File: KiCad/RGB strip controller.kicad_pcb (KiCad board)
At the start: 2 copper layers, 17.1 x 48.9 mm, 16 parts, among them J1 USB_C_Receptacle_USB2.0, J2 Conn_01x03, SW1 SW_SPST, U1 ESP-01, U2 LM317_TO-220

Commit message: PCB revision 2
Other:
- board text added: "v2"
- board text added: "←"

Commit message: PCB v3
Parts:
- added U3: TC7SZ125FU, Package_TO_SOT_SMD:SOT-353_SC-70-5, F.Cu at (182.8, 68.3)
- C1: footprint Capacitor_THT:C_Radial_D5.0mm_H11.0mm_P2.00mm -> Capacitor_SMD:C_1206_3216Metric
- C2, C4: footprint Capacitor_THT:C_Disc_D3.0mm_W1.6mm_P2.50mm -> Capacitor_SMD:C_0603_1608Metric
- C3: footprint Capacitor_THT:C_Radial_D5.0mm_H11.0mm_P2.00mm -> Capacitor_SMD:C_0603_1608Metric
- D1: footprint Diode_THT:D_A-405_P7.62mm_Horizontal -> Diode_SMD:D_SOD-123F
- R1, R2, R3, R4, R5, R6: footprint Resistor_THT:R_Axial_DIN0207_L6.3mm_D2.5mm_P7.62mm_Horizontal -> Resistor_SMD:R_0402_1005Metric
- moved R4 56.1 mm to (182.8, 70.6), turned to 180 degrees
- moved R5 55.5 mm to (181.6, 88.0)
- moved R1 53.3 mm to (183.6, 88.0), turned to 180 degrees
- moved R3 50.0 mm to (176.4, 88.0), turned to 180 degrees
- moved U2 48.6 mm to (176.4, 79.6)
- moved J1 47.3 mm to (179.1, 94.0)
- moved D1 46.7 mm to (181.4, 65.3)
- moved R6 46.3 mm to (179.1, 88.0), turned to 0 degrees
- moved J2 45.6 mm to (176.4, 62.2)
- moved C4 45.1 mm to (182.7, 75.4)
- moved C2 45.0 mm to (182.7, 72.1)
- moved U1 44.8 mm to (175.3, 83.1)
- moved C3 43.7 mm to (182.7, 73.8), turned to 0 degrees
- moved SW1 42.7 mm to (179.6, 68.1)
- moved C1 37.5 mm to (176.6, 65.3), turned to 180 degrees
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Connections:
- J2 pad 2: LED_Data -> Net-(J2-Pad2)
- R4 pad 1: LED_Data -> Net-(R4-Pad1)
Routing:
- net GND: track 2.90 -> 69.4 mm, vias 0 -> 3
- net LED_Data: track 22.7 -> 0.00 mm
- net Net-(R5-Pad1): track 7.29 -> 23.3 mm, vias 0 -> 2
- net Net-(R1-Pad1): track 19.6 -> 7.97 mm, vias 0 -> 1
- net Net-(R4-Pad2): track 12.0 -> 21.9 mm
- net Net-(J2-Pad2): track 0.00 -> 7.48 mm, vias 0 -> 1
- net +3V3: track 39.8 -> 46.8 mm, vias 0 -> 3
- net Net-(SW1-Pad2): track 10.3 -> 16.4 mm
- net +5V: track 59.8 -> 64.8 mm, vias 0 -> 5
- net Net-(J1-PadA5): track 6.25 -> 2.30 mm
- net Net-(J1-PadB5): track 5.38 -> 9.09 mm, vias 0 -> 2
- net Net-(R4-Pad1): track 0.00 -> 1.55 mm
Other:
- board size 17.1 x 48.9 mm -> 11.6 x 38.6 mm
- board text added: "(>w<)"
- board text added: "actually 300 and 470"
- board text added: "v3"
- board text removed: "-"
- board text removed: "v2"
- board text removed: "←"

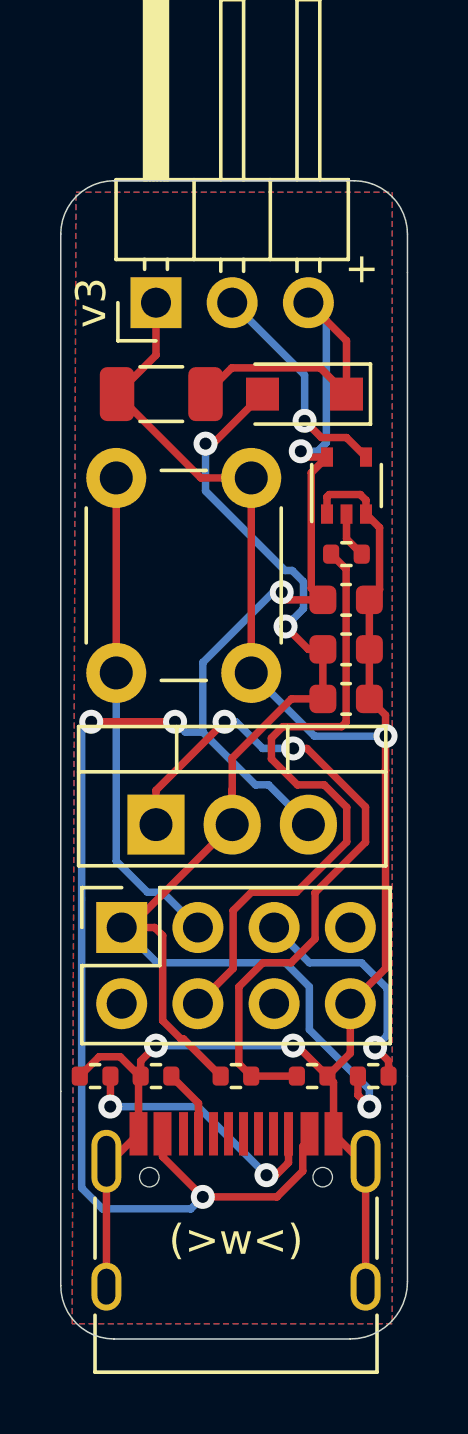
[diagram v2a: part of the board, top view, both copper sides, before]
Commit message: Update to KiCad 6
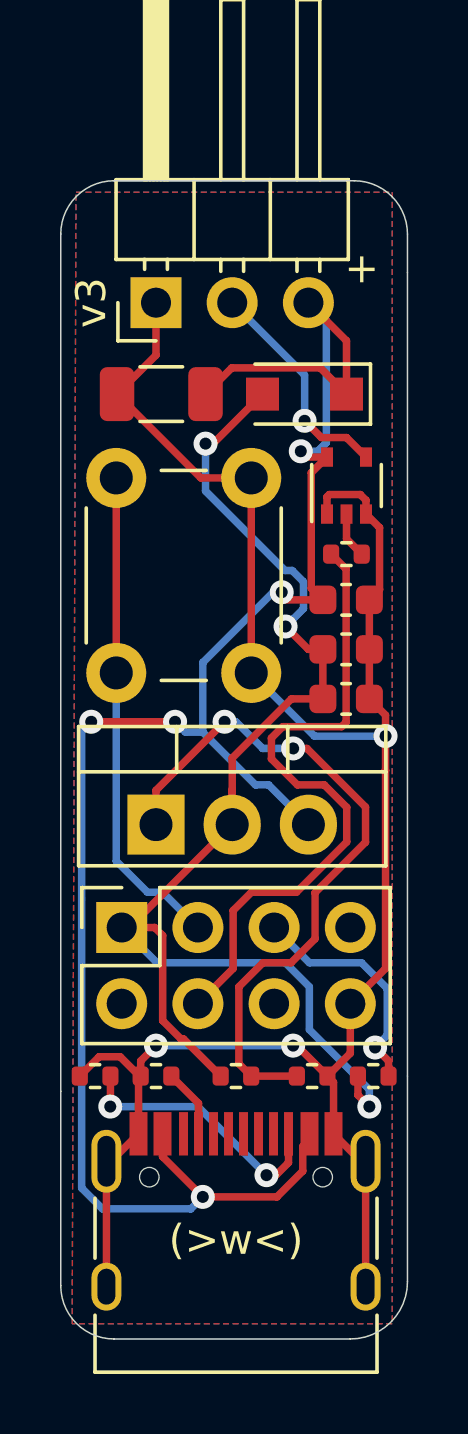
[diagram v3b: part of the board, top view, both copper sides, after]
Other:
- net class Default removed

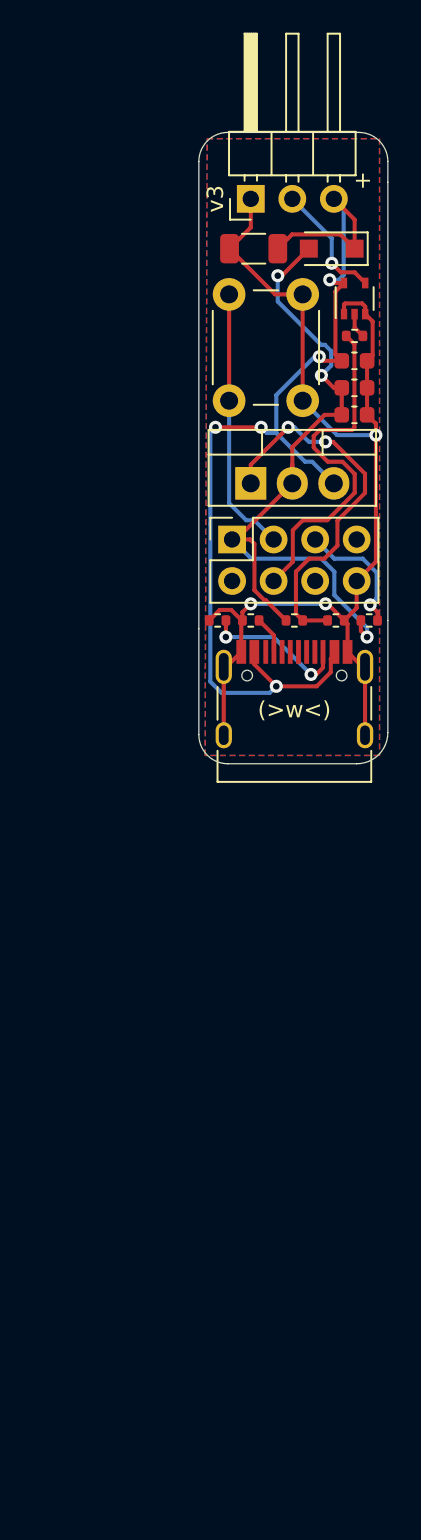
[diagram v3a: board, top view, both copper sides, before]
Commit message: Redo PCB to suck slightly less
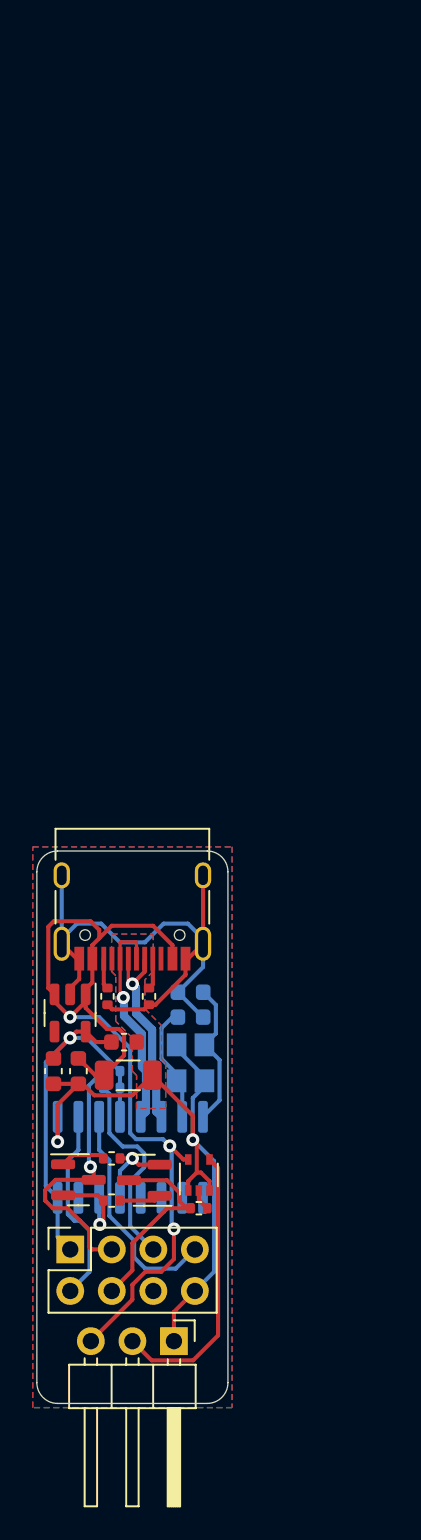
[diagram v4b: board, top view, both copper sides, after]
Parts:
- removed D1: 1N4001, Diode_SMD:D_SOD-123F
- removed R5: 400, Resistor_SMD:R_0402_1005Metric
- removed R6: 240, Resistor_SMD:R_0402_1005Metric
- removed SW1: SW_SPST, Button_Switch_THT:SW_PUSH_6mm_H5mm
- added C5: 22p, Capacitor_SMD:C_0603_1608Metric, B.Cu at (172.7, 112.3)
- added C6: 22p, Capacitor_SMD:C_0603_1608Metric, B.Cu at (172.7, 110.7)
- added Q1: BC847, Package_TO_SOT_SMD:SOT-23, F.Cu at (165.9, 122.2)
- added Q2: BC847, Package_TO_SOT_SMD:SOT-23, F.Cu at (169.9, 122.2)
- added R7: 10k, Resistor_SMD:R_0402_1005Metric, B.Cu at (167.9, 115.6)
- added R8: 10k, Resistor_SMD:R_0402_1005Metric, F.Cu at (167.9, 120.9)
- added R9: 10k, Resistor_SMD:R_0402_1005Metric, F.Cu at (167.9, 123.5)
- added U4: CH340G, Package_SO:SOIC-16_3.9x9.9mm_P1.27mm, B.Cu at (169.0, 120.8)
- added Y1: 12M, Crystal:Crystal_SMD_3225-4Pin_3.2x2.5mm, B.Cu at (172.7, 115.1)
- R1: moved to B.Cu
- U2: value LM317_TO-220 -> SPX3819M5-L-3-3; footprint Package_TO_SOT_THT:TO-220-3_Vertical -> Package_TO_SOT_SMD:SOT-23-5
- moved J2 70.0 mm to (171.7, 132.1), turned to -90 degrees
- moved U3 54.4 mm to (173.2, 121.9)
- moved R4 54.2 mm to (173.2, 124.0)
- moved C1 51.1 mm to (168.9, 115.8), turned to 0 degrees
- moved C2 46.6 mm to (165.9, 115.6), turned to -90 degrees
- moved U1 44.5 mm to (165.4, 126.5)
- moved C4 44.1 mm to (164.3, 115.6), turned to -90 degrees
- moved C3 42.4 mm to (168.7, 113.8)
- moved U2 34.2 mm to (165.4, 112.0), turned to -90 degrees
- moved R1 32.6 mm to (167.9, 116.6), turned to 0 degrees
- moved R2 24.0 mm to (167.6, 111.0), turned to -90 degrees
- moved R3 23.8 mm to (170.2, 111.0), turned to -90 degrees
- moved J1 14.6 mm to (169.2, 104.6), turned to 180 degrees
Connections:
- net Net-(J1-PadA5) renamed /CC1
- net Net-(J1-PadB5) renamed /CC2
- net Net-(J2-Pad2) renamed RGB_D
- net Net-(R1-Pad1) renamed /EN
- net Net-(R4-Pad2) renamed IO0
- J1 pad A6: Net-(J1-PadA6) -> D+
- J1 pad A7: Net-(J1-PadA7) -> D-
- J1 pad A8: Net-(J1-PadA8) -> unconnected-(J1-PadA8)
- J1 pad B6: Net-(J1-PadB6) -> D+
- J1 pad B7: Net-(J1-PadB7) -> D-
- J1 pad B8: Net-(J1-PadB8) -> unconnected-(J1-PadB8)
- U1 pad 2: Net-(U1-Pad2) -> TX
- U1 pad 3: Net-(SW1-Pad2) -> RST
- U1 pad 6: Net-(U1-Pad6) -> unconnected-(U1-Pad6)
- U1 pad 7: Net-(U1-Pad7) -> RX
- U2 pad 1: Net-(R5-Pad1) -> +5V
- U2 pad 2: +3V3 -> GND
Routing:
- net Net-(R5-Pad1): track 23.3 -> 0.00 mm, vias 2 -> 0
- net +3V3: track 46.8 -> 25.5 mm, vias 3 -> 1
- net RST: track 0.00 -> 16.9 mm, vias 0 -> 1
- net Net-(SW1-Pad2): track 16.4 -> 0.00 mm
- net D+: track 0.00 -> 14.2 mm, vias 0 -> 1
- net RX: track 0.00 -> 14.0 mm
- net D-: track 0.00 -> 13.4 mm, vias 0 -> 1
- net TX: track 0.00 -> 12.2 mm
- net GND: track 69.4 -> 80.2 mm, vias 3 -> 2
- net RGB_D: track 7.48 -> 17.3 mm, vias 1 -> 0
- net IO0: track 21.9 -> 12.7 mm
- net /XO: track 0.00 -> 9.03 mm
- net /XI: track 0.00 -> 7.23 mm
- net /CC2: track 9.09 -> 1.89 mm, vias 2 -> 0
- net RTS: track 0.00 -> 5.79 mm, vias 0 -> 1
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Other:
- board size 11.6 x 38.6 mm -> 11.7 x 33.8 mm
- board text removed: "(>w<)"
- board text removed: "+"
- board text removed: "actually 300 and 470"
- board text removed: "v3"

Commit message: Finalize v4 PCB
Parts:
- added G***: umbreon_2layer_6mm, _Project:umbreon_2layer_6mm, B.Cu at (170.4, 135.4)
- added REF**: OSHW-Logo2_7.3x6mm_SilkScreen, Symbol:OSHW-Logo2_7.3x6mm_SilkScreen, B.Cu at (171.2, 129.5)
- moved J1 32.1 mm to (170.6, 136.7), turned to 0 degrees
- moved J2 23.1 mm to (168.1, 109.3), turned to 90 degrees
- moved C6 20.7 mm to (167.1, 130.6), turned to 0 degrees
- moved R2 19.9 mm to (172.1, 130.4), turned to 90 degrees
- moved U2 19.6 mm to (174.4, 129.3), turned to 90 degrees
- moved R3 19.4 mm to (169.6, 130.4), turned to 90 degrees
- moved C5 17.8 mm to (167.1, 129.1), turned to 180 degrees
- moved C4 15.1 mm to (175.4, 125.8), turned to 90 degrees
- moved U1 14.7 mm to (174.4, 114.9), turned to -90 degrees
- moved C3 14.0 mm to (171.1, 127.6), turned to 180 degrees
- moved C2 13.0 mm to (173.9, 125.8), turned to 90 degrees
- moved Y1 12.6 mm to (167.1, 126.3), turned to -90 degrees
- moved R7 11.0 mm to (171.9, 125.8), turned to 180 degrees
- moved C1 9.91 mm to (170.9, 125.5), turned to 180 degrees
- moved R4 9.35 mm to (166.6, 117.4), turned to 0 degrees
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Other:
- board text added: "(>w<)"
- board text added: "(^.^)"
- board text added: "+"
- board text added: "2022.10.04"
- board text added: "<.<"
- board text added: ">.>"
- board text added: "JLCJLCJLCJLC"
- board text added: "archive.eritbh.me/rgb"
- board text added: "trans rights!"
- board text added: "v4"
- board text added: "→"
